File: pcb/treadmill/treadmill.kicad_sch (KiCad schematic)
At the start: 34 parts, among them J1 EXT_SERIAL?, J2 TO_MOTOR_BOARD, J3 PRG, J4 PRG2, J5 KEY, Q1 "2T1" SS9012 PNP, Q2 "J3" SS9013 NPN, U1 STM8S005K6T6C, U2 LM78M05_TO252, U3 PL51WT020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

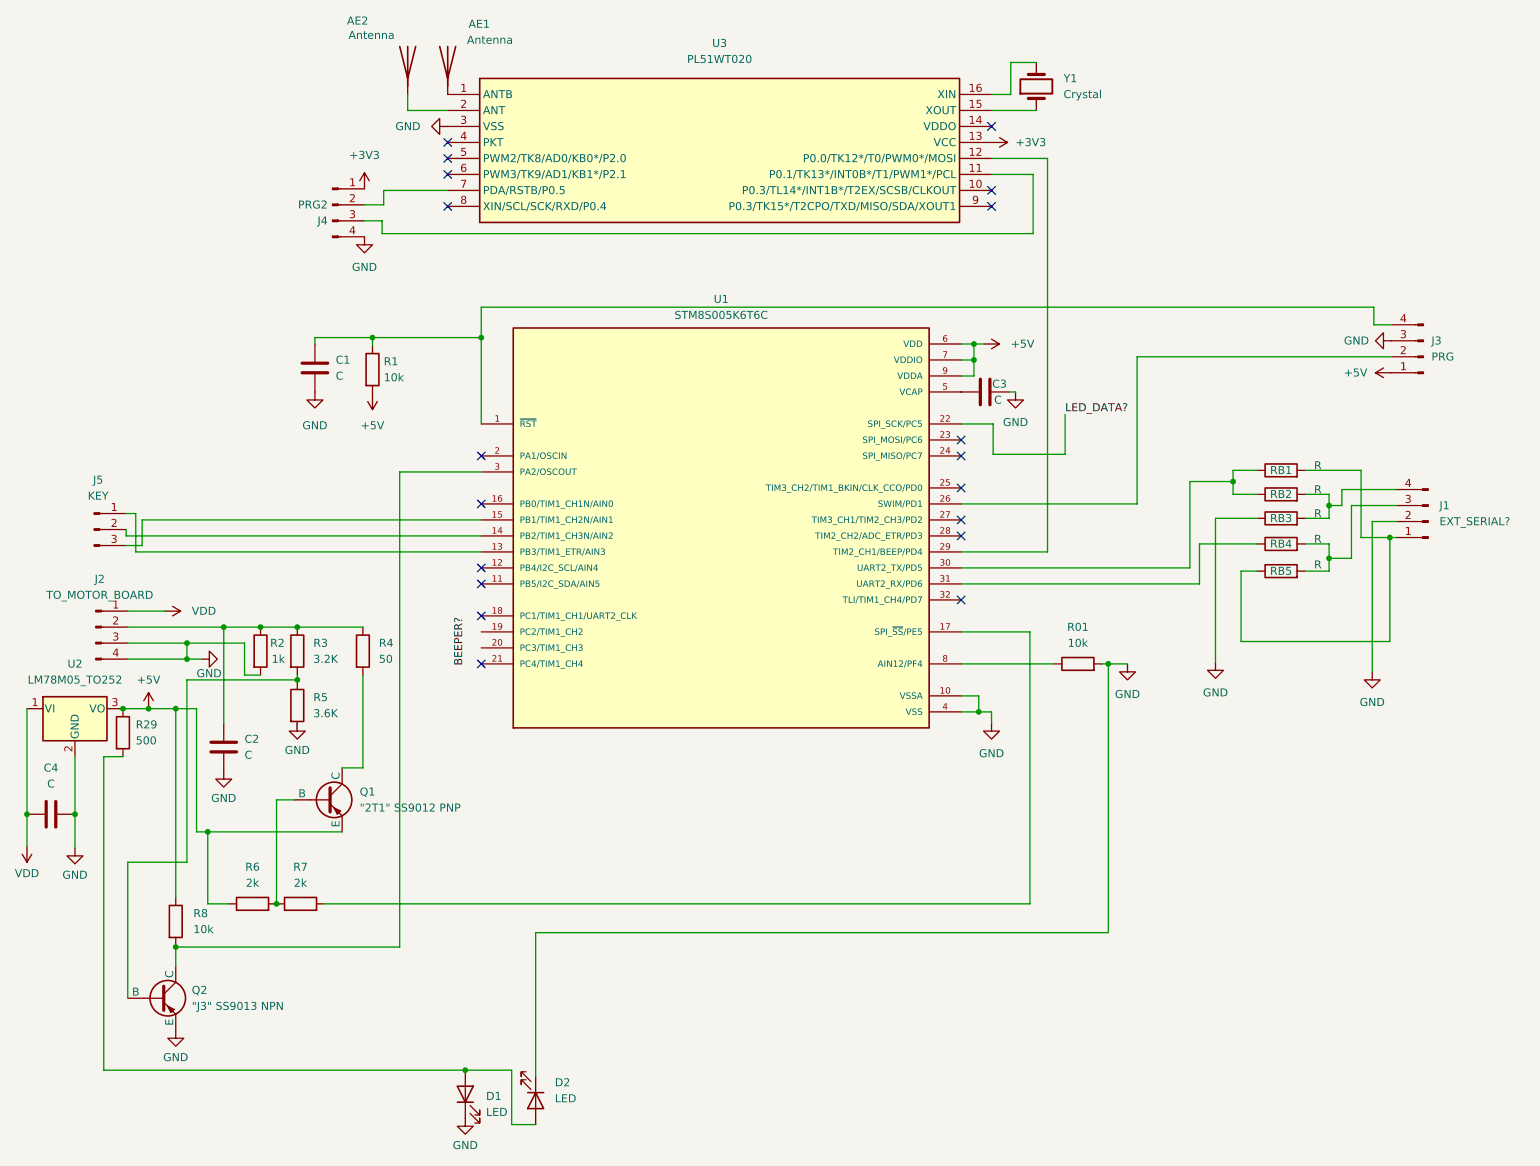
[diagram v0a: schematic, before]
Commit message: Add more datasheets for components in control board. More pcb reversing in control board and separate them with hierarchical sheets.
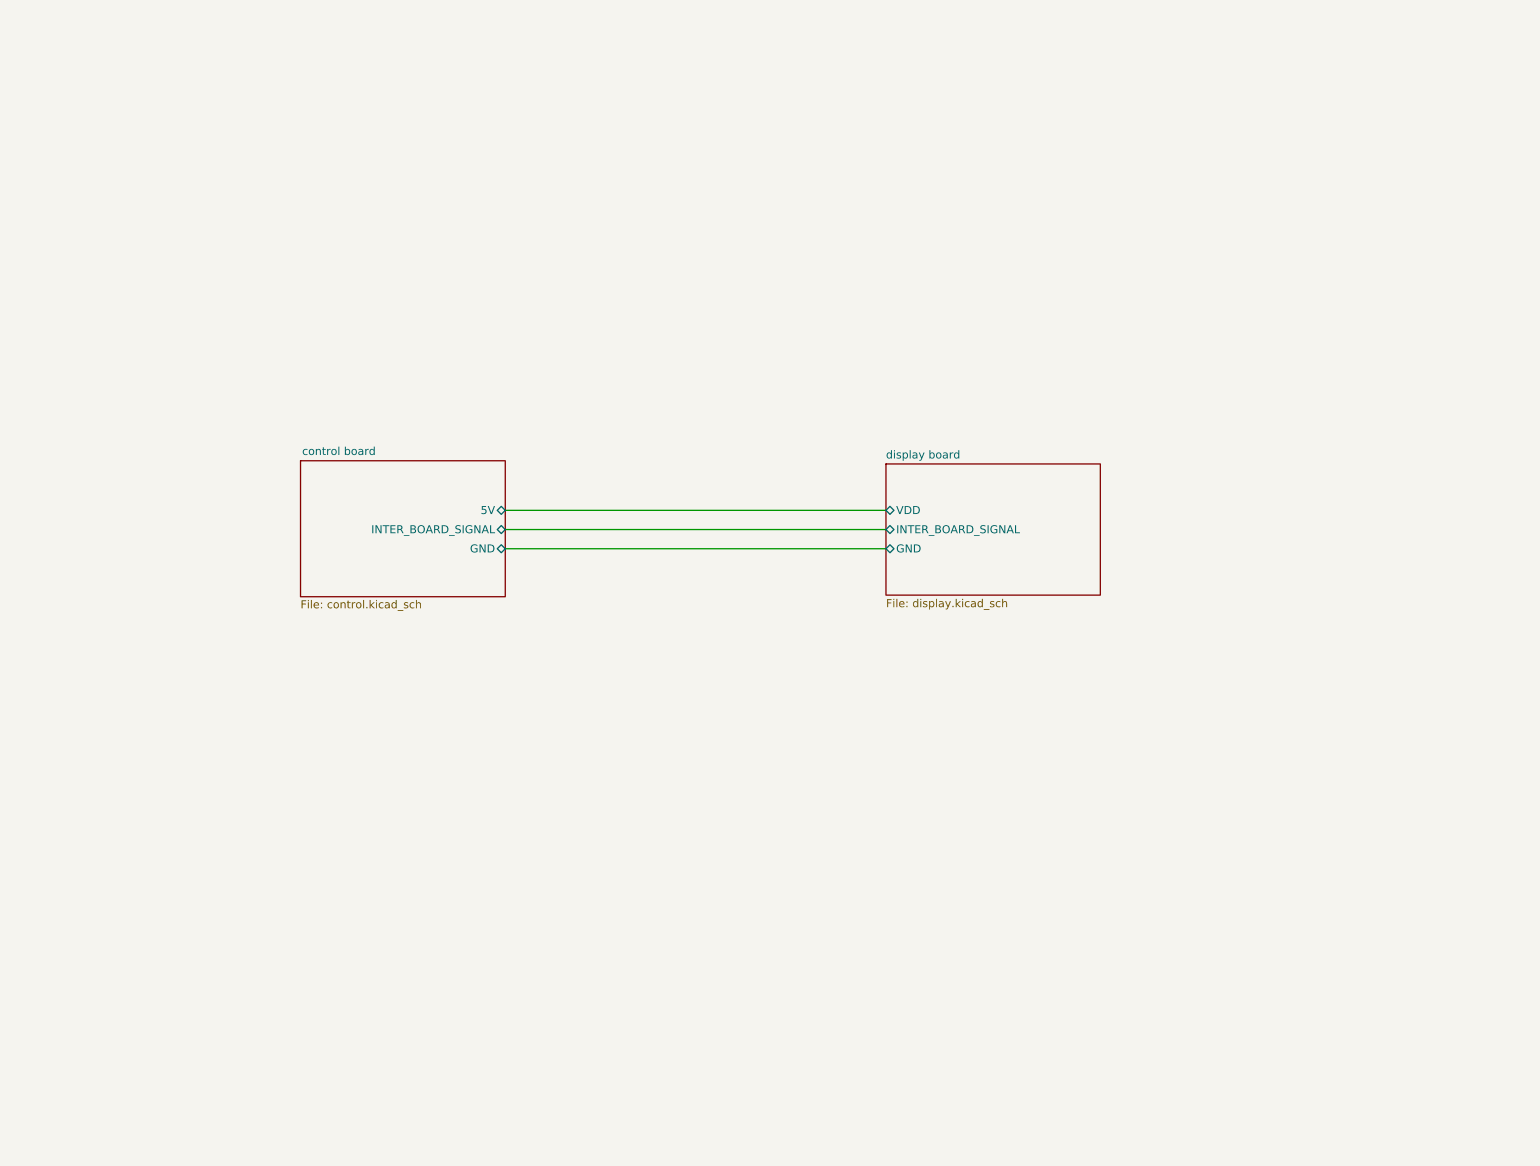
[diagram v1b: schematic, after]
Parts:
- removed AE1, AE2: Antenna, symbol Device:Antenna
- removed C1, C2, C3, C4: C, symbol Device:C
- removed D1, D2: LED, symbol Device:LED
- removed J1: EXT_SERIAL?, symbol Connector:Conn_01x04_Pin
- removed J2: TO_MOTOR_BOARD, symbol Connector:Conn_01x04_Pin
- removed J3: PRG, symbol Connector:Conn_01x04_Pin
- removed J4: PRG2, symbol Connector:Conn_01x04_Pin
- removed J5: KEY, symbol Connector:Conn_01x03_Pin
- removed Q1: "2T1" SS9012 PNP, symbol Simulation_SPICE:PNP
- removed Q2: "J3" SS9013 NPN, symbol Simulation_SPICE:PNP
- removed R01, R1, R8: 10k, symbol Device:R
- removed R2: 1k, symbol Device:R
- removed R29: 500, symbol Device:R
- removed R3: 3.2K, symbol Device:R
- removed R4: 50, symbol Device:R
- removed R5: 3.6K, symbol Device:R
- removed R6, R7: 2k, symbol Device:R
- removed RB1, RB2, RB3, RB4, RB5: R, symbol Device:R
- removed U1: STM8S005K6T6C, STM8S005K6T6C:QFP80P900X900X160-32N, symbol stm8005k6:STM8S005K6T6C
- removed U2: LM78M05_TO252, Package_TO_SOT_SMD:TO-252-2, symbol Regulator_Linear:LM78M05_TO252
- removed U3: PL51WT020, symbol pl51wt020:PL51WT020
- removed Y1: Crystal, symbol Device:Crystal
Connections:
- no-connect marks 19 -> 0
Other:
- added sheet control board (control.kicad_sch)
- added sheet display board (display.kicad_sch)
